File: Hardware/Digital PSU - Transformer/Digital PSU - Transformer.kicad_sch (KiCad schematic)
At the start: 10 parts, among them J10 18V AC, J11 18V AC, J4 15V AC, J5 230V AC

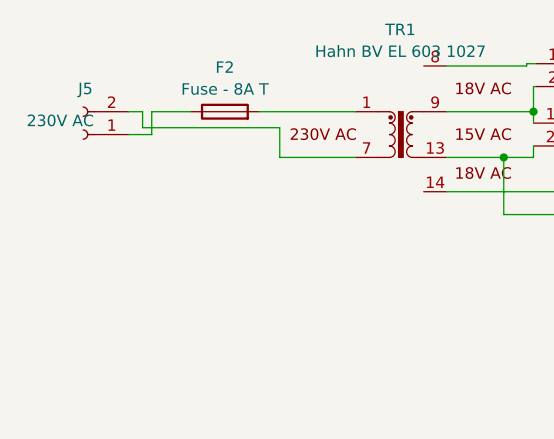
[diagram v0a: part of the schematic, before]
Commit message: Ready for review (updated Digital PSU - Transformer and Controller)
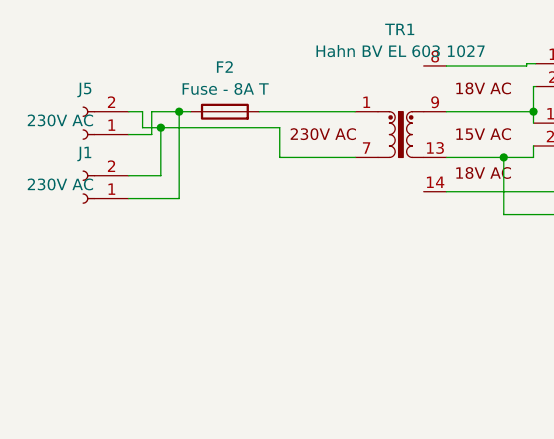
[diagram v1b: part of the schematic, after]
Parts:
- added J1: 230V AC, THE_PREAMP_CONN_POWER_5_08:TBP01R1-508-02BK, symbol Connector:Conn_01x02_Socket
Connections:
- net at F2.1, J5.1 (Pin_1): now also J1.1 (Pin_1)
- net at J5.2 (Pin_2), TR1.7: now also J1.2 (Pin_2)
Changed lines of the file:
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@@
+	)
+	(junction
+		(at 67.31 98.806)
+		(diameter 0)
+		(color 0 0 0 0)
 	)
 	(junction
@@
 		(color 0 0 0 0)
 	)
+	(junction
+		(at 65.278 100.584)
+		(diameter 0)
+		(color 0 0 0 0)
+	)
+	(wire
+		(pts
+			(xy 65.278 105.918) (xy 65.278 100.584)
+		)
+		(stroke
+			(width 0)
+			(type default)
+		)
+	)
 	(wire
 		(pts
@@
 	(wire
 		(pts
-			(xy 64.262 98.806) (xy 68.58 98.806)
+			(xy 67.31 98.806) (xy 68.58 98.806)
+		)
+		(stroke
+			(width 0)
+			(type default)
+		)
+	)
+	(wire
+		(pts
+			(xy 64.262 98.806) (xy 67.31 98.806)
 		)
 		(stroke
@@
 	(wire
 		(pts
+			(xy 67.31 108.458) (xy 67.31 98.806)
+		)
+		(stroke
+			(width 0)
+			(type default)
+		)
+	)
+	(wire
+		(pts
 			(xy 76.2 98.806) (xy 86.868 98.806)
 		)
@@
 	(wire
 		(pts
+			(xy 61.722 108.458) (xy 67.31 108.458)
+		)
+		(stroke
+			(width 0)
+			(type default)
+		)
+	)
+	(wire
+		(pts
 			(xy 78.486 103.886) (xy 86.868 103.886)
 		)
@@
 	(wire
 		(pts
+			(xy 65.278 100.584) (xy 78.486 100.584)
+		)
+		(stroke
+			(width 0)
+			(type default)
+		)
+	)
+	(wire
+		(pts
 			(xy 61.722 101.346) (xy 64.262 101.346)
 		)
@@
 	(wire
 		(pts
-			(xy 63.246 100.584) (xy 78.486 100.584)
+			(xy 63.246 100.584) (xy 65.278 100.584)
+		)
+		(stroke
+			(width 0)
+			(type default)
+		)
+	)
+	(wire
+		(pts
+			(xy 61.722 105.918) (xy 65.278 105.918)
 		)
 		(stroke
@@
 					(unit 1)
 				)
+			)
+		)
+	)
+	(symbol
+		(lib_id "Connector:Conn_01x02_Socket")
+		(at 56.642 108.458 180)
+		(unit 1)
+		(exclude_from_sim no)
+		(in_bom yes)
+		(on_board yes)
+		(dnp no)
+		(property "Reference" "J1"
+			(at 56.896 103.378 0)
+			(effects
+				(font
+					(size 1.27 1.27)
+				)
+			)
+		)
+		(property "Value" "230V AC"
+			(at 54.102 106.934 0)
+			(effects
+				(font
+					(size 1.27 1.27)
+				)
+			)
+		)
+		(property "Footprint" "THE_PREAMP_CONN_POWER_5_08:TBP01R1-508-02BK"
+			(at 56.642 108.458 0)
+			(effects
+				(font
+					(size 1.27 1.27)
+				)
+				(hide yes)
+			)
+		)
+		(property "Datasheet" "~"
+			(at 56.642 108.458 0)
+			(effects
+				(font
+					(size 1.27 1.27)
+				)
+				(hide yes)
+			)
+		)
+		(property "Description" "Generic connector, single row, 01x02, script generated"
+			(at 56.642 108.458 0)
+			(effects
+				(font
+					(size 1.27 1.27)
+				)
+				(hide yes)
+			)
+		)
+		(pin "1"
+		)
+		(pin "2"
+		)
+		(instances
+			(project "Digital PSU - Transformer"
+				(path "/5cc6b3bf-721e-4dc8-af0a-72c27b8cc795"
+					(reference "J1")
+					(unit 1)
+				)
